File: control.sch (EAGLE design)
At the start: 4 parts, among them IC1 L293D, U1 AL5802-7, U4 AL5802-7

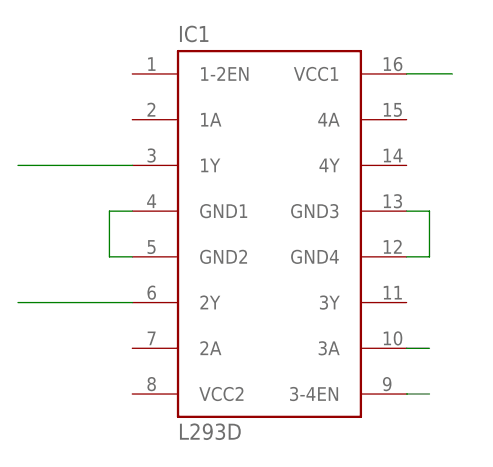
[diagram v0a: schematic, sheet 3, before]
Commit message: adds h bridge wirirng
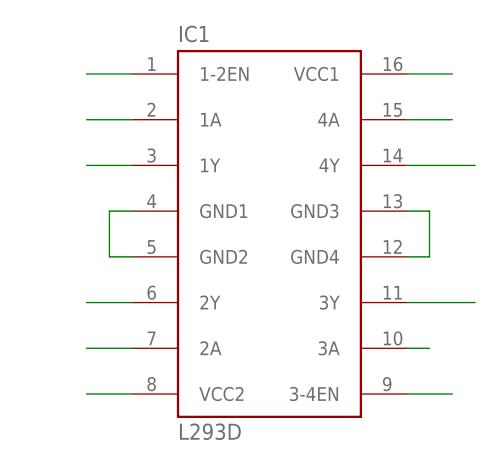
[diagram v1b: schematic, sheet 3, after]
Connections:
- net N$1 renamed M1A
- net N$6 renamed M1B
- net N$8 renamed SPEED2
- net N$9 renamed DIR2B
- new net DIR1A: IC1.1A
- new net DIR1B: IC1.2A
- new net DIR2A: IC1.4A
- new net M2A: IC1.4Y
- new net M2B: IC1.3Y
- new net SPEED1: IC1.1-2EN
- net 24V: now also IC1.VCC2
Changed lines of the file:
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@@
 </segment>
 </net>
-<net name="N$1" class="0">
+<net name="M1A" class="0">
 <segment>
 <pinref part="IC1" gate="G$1" pin="1Y"/>
-<wire x1="-5.08" y1="27.94" x2="-17.78" y2="27.94" width="0.1524" layer="91"/>
+<wire x1="-5.08" y1="27.94" x2="-10.16" y2="27.94" width="0.1524" layer="91"/>
 </segment>
 </net>
-<net name="N$6" class="0">
+<net name="M1B" class="0">
 <segment>
 <pinref part="IC1" gate="G$1" pin="2Y"/>
-<wire x1="-5.08" y1="12.7" x2="-17.78" y2="12.7" width="0.1524" layer="91"/>
+<wire x1="-5.08" y1="12.7" x2="-10.16" y2="12.7" width="0.1524" layer="91"/>
 </segment>
 </net>
-<net name="N$8" class="0">
+<net name="SPEED2" class="0">
 <segment>
 <pinref part="IC1" gate="G$1" pin="3-4EN"/>
-<wire x1="25.4" y1="2.54" x2="27.94" y2="2.54" width="0.1524" layer="91"/>
+<wire x1="25.4" y1="2.54" x2="30.48" y2="2.54" width="0.1524" layer="91"/>
 </segment>
 </net>
-<net name="N$9" class="0">
+<net name="DIR2B" class="0">
 <segment>
 <pinref part="IC1" gate="G$1" pin="3A"/>
@@
 </segment>
 </net>
+<net name="24V" class="0">
+<segment>
+<pinref part="IC1" gate="G$1" pin="VCC2"/>
+<wire x1="-5.08" y1="2.54" x2="-10.16" y2="2.54" width="0.1524" layer="91"/>
+</segment>
+</net>
+<net name="M2A" class="0">
+<segment>
+<pinref part="IC1" gate="G$1" pin="4Y"/>
+<wire x1="25.4" y1="27.94" x2="33.02" y2="27.94" width="0.1524" layer="91"/>
+</segment>
+</net>
+<net name="M2B" class="0">
+<segment>
+<pinref part="IC1" gate="G$1" pin="3Y"/>
+<wire x1="25.4" y1="12.7" x2="33.02" y2="12.7" width="0.1524" layer="91"/>
+</segment>
+</net>
+<net name="SPEED1" class="0">
+<segment>
+<pinref part="IC1" gate="G$1" pin="1-2EN"/>
+<wire x1="-5.08" y1="38.1" x2="-10.16" y2="38.1" width="0.1524" layer="91"/>
+</segment>
+</net>
+<net name="DIR1A" class="0">
+<segment>
+<pinref part="IC1" gate="G$1" pin="1A"/>
+<wire x1="-5.08" y1="33.02" x2="-10.16" y2="33.02" width="0.1524" layer="91"/>
+</segment>
+</net>
+<net name="DIR2A" class="0">
+<segment>
+<pinref part="IC1" gate="G$1" pin="4A"/>
+<wire x1="25.4" y1="33.02" x2="30.48" y2="33.02" width="0.1524" layer="91"/>
+</segment>
+</net>
+<net name="DIR1B" class="0">
+<segment>
+<pinref part="IC1" gate="G$1" pin="2A"/>
+<wire x1="-5.08" y1="7.62" x2="-10.16" y2="7.62" width="0.1524" layer="91"/>
+</segment>
+</net>

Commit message: adds LED driver
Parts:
- removed IC1: L293D, st-microelectronics:L293D
- removed U1, U4: AL5802-7, LED Driver:AL5802-7
- added C1: UVR0J102MPD1TA, Smile_Shade:UVR0J102MPD1TA
- added C2: ESK107M025AE3EA, Smile_Shade:ESK107M025AE3EA
- added R1, R10, R11, R12, R13, R14, R15, R16, R2, R3, R4, R5, R6, R7, R8, R9: RC0603FR-0710RL, LED Driver:RC0603FR-0710RL
- added U$10, U$12, U$14, U$16, U$18, U$20, U$22, U$24, U$26, U$28, U$30, U$32, U$34, U$4, U$6, U$8: 2N7002P, LED Driver:2N7002P
- added U$11, U$13, U$15, U$17, U$19, U$21, U$23, U$25, U$27, U$29, U$3, U$31, U$33, U$5, U$7, U$9: NUD4011DR2G, LED Driver:NUD4011DR2G
- added U$2: L293DNE, LED Driver:L293DNE
- added U$35: LM2576HVT-5.0/NOPB, LED Driver:LM2576HVT-5.0/NOPB
- added U$36: SRN8040-101M, Smile_Shade:SRN8040-101M
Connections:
- removed net DIR1B: IC1.2A
- removed net DIR2A: IC1.4A
- removed net DIR2B: IC1.3A
- removed net LED1: U1.OUT
- removed net M1A: IC1.1Y
- removed net M2B: IC1.3Y
- removed net SPEED1: IC1.1-2EN
- removed net SPEED2: IC1.3-4EN
- new net 48V: C2.11, R1.22, R10.22, R11.22, R12.22, R13.22, R14.22, R15.22, R16.22, R2.22, R3.22, R4.22, R5.22, R6.22, R7.22, R8.22, R9.22, U$11.VIN, U$13.VIN, U$15.VIN, U$17.VIN, U$19.VIN, U$21.VIN, U$23.VIN, U$25.VIN, U$27.VIN, U$29.VIN, U$3.VIN, U$31.VIN, U$33.VIN, U$5.VIN, U$7.VIN, U$9.VIN
- new net LEDSTR_1: U$17.LED1, U$17.LED2, U$17.LED3, U$17.LED4
- new net LEDSTR_10: U$21.LED1, U$21.LED2, U$21.LED3, U$21.LED4
- new net LEDSTR_11: U$23.LED1, U$23.LED2, U$23.LED3, U$23.LED4
- new net LEDSTR_12: U$25.LED1, U$25.LED2, U$25.LED3, U$25.LED4
- new net LEDSTR_13: U$27.LED1, U$27.LED2, U$27.LED3, U$27.LED4
- new net LEDSTR_14: U$29.LED1, U$29.LED2, U$29.LED3, U$29.LED4
- new net LEDSTR_15: U$31.LED1, U$31.LED2, U$31.LED3, U$31.LED4
- new net LEDSTR_16: U$33.LED1, U$33.LED2, U$33.LED3, U$33.LED4
- new net LEDSTR_2: U$3.LED1, U$3.LED2, U$3.LED3, U$3.LED4
- new net LEDSTR_3: U$5.LED1, U$5.LED2, U$5.LED3, U$5.LED4
- new net LEDSTR_4: U$7.LED1, U$7.LED2, U$7.LED3, U$7.LED4
- new net LEDSTR_5: U$9.LED1, U$9.LED2, U$9.LED3, U$9.LED4
- new net LEDSTR_6: U$11.LED1, U$11.LED2, U$11.LED3, U$11.LED4
- new net LEDSTR_7: U$13.LED1, U$13.LED2, U$13.LED3, U$13.LED4
- new net LEDSTR_8: U$15.LED1, U$15.LED2, U$15.LED3, U$15.LED4
- new net LEDSTR_9: U$19.LED1, U$19.LED2, U$19.LED3, U$19.LED4
- new net N$1: U$3.PWM, U$4.SOURCE
- new net N$10: R5.11, U$11.REXT
- new net N$11: U$13.PWM, U$14.SOURCE
- new net N$12: R6.11, U$13.REXT
- new net N$13: U$15.PWM, U$16.SOURCE
- new net N$14: R7.11, U$15.REXT
- new net N$15: U$17.PWM, U$18.SOURCE
- new net N$16: R8.11, U$17.REXT
- new net N$17: U$19.PWM, U$20.SOURCE
- new net N$18: R9.11, U$19.REXT
- new net N$19: U$21.PWM, U$22.SOURCE
- new net N$20: R10.11, U$21.REXT
- new net N$21: U$23.PWM, U$24.SOURCE
- new net N$22: R11.11, U$23.REXT
- new net N$23: U$25.PWM, U$26.SOURCE
- new net N$24: R12.11, U$25.REXT
- new net N$25: U$27.PWM, U$28.SOURCE
- new net N$26: R13.11, U$27.REXT
- new net N$27: U$29.PWM, U$30.SOURCE
- new net N$28: R14.11, U$29.REXT
- new net N$29: U$31.PWM, U$32.SOURCE
- new net N$30: R15.11, U$31.REXT
- new net N$31: U$33.PWM, U$34.SOURCE
- new net N$32: R16.11, U$33.REXT
- new net N$33: U$35.OUT, U$36.1
- new net N$34: C2.22, U$35.VIN
- new net N$6: R3.11, U$7.REXT
- new net N$8: R4.11, U$9.REXT
- new net N$9: U$11.PWM, U$12.SOURCE
- new net PWMLED1: U$4.GATE
- new net PWMLED10: U$22.GATE
- new net PWMLED11: U$24.GATE
- new net PWMLED12: U$26.GATE
- new net PWMLED13: U$28.GATE
- new net PWMLED14: U$30.GATE
- new net PWMLED15: U$32.GATE
- new net PWMLED16: U$34.GATE
- new net PWMLED2: U$6.GATE
- new net PWMLED3: U$8.GATE
- new net PWMLED4: U$10.GATE
- new net PWMLED5: U$12.GATE
- new net PWMLED6: U$14.GATE
- new net PWMLED7: U$16.GATE
- new net PWMLED8: U$18.GATE
- new net PWMLED9: U$20.GATE
- net 24V: now also U$2.VCC2; no longer IC1.VCC2, U1.BIAS, U4.BIAS
- net 5V: now also C1.22, U$1.CHG-IN, U$2.VCC1, U$35.FB, U$36.2; no longer IC1.VCC1
- net DIR1A: now also U$2.2A; no longer IC1.1A
- net GND: now also C1.11, U$10.DRAIN, U$12.DRAIN, U$14.DRAIN, U$16.DRAIN, U$18.DRAIN, U$2.HEATSINKANDGROUND, U$2.HEATSINKANDGROUND_2, U$2.HEATSINKANDGROUND_3, U$2.HEATSINKANDGROUND_4, U$20.DRAIN, U$22.DRAIN, U$24.DRAIN, U$26.DRAIN, U$28.DRAIN, U$30.DRAIN, U$32.DRAIN, U$34.DRAIN, U$35.!ON/OFF, U$35.GND, U$4.DRAIN, U$6.DRAIN, U$8.DRAIN; no longer IC1.GND1, IC1.GND2, IC1.GND3, IC1.GND4, U1.GND, U4.GND
- net M1B: now also U$2.2Y; no longer IC1.2Y
- net M2A: now also U$2.4Y; no longer IC1.4Y
- net N$2: now also R1.11, U$3.REXT; no longer U4.FB, U4.REXT
- net N$3: now also U$5.PWM, U$6.SOURCE; no longer U1.FB, U1.REXT
- net N$4: now also R2.11, U$5.REXT; no longer U4.EN
- net N$5: now also U$7.PWM, U$8.SOURCE; no longer U1.EN
- net N$7: now also U$10.SOURCE, U$9.PWM; no longer U4.OUT

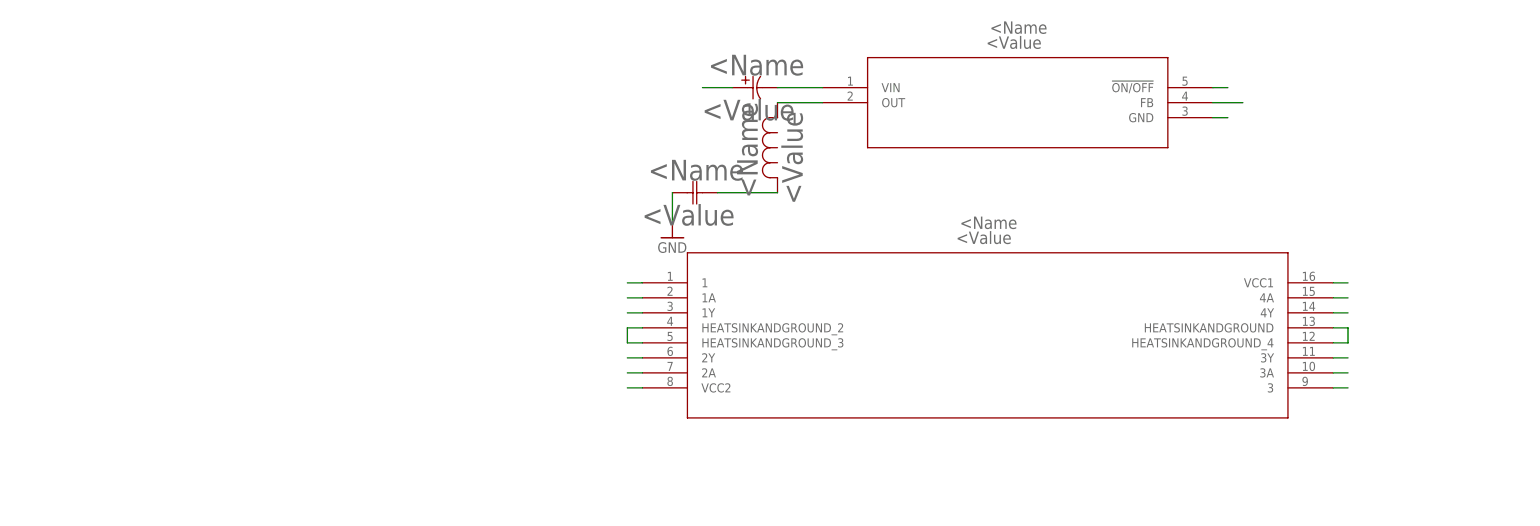
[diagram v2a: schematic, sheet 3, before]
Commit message: adds PWM
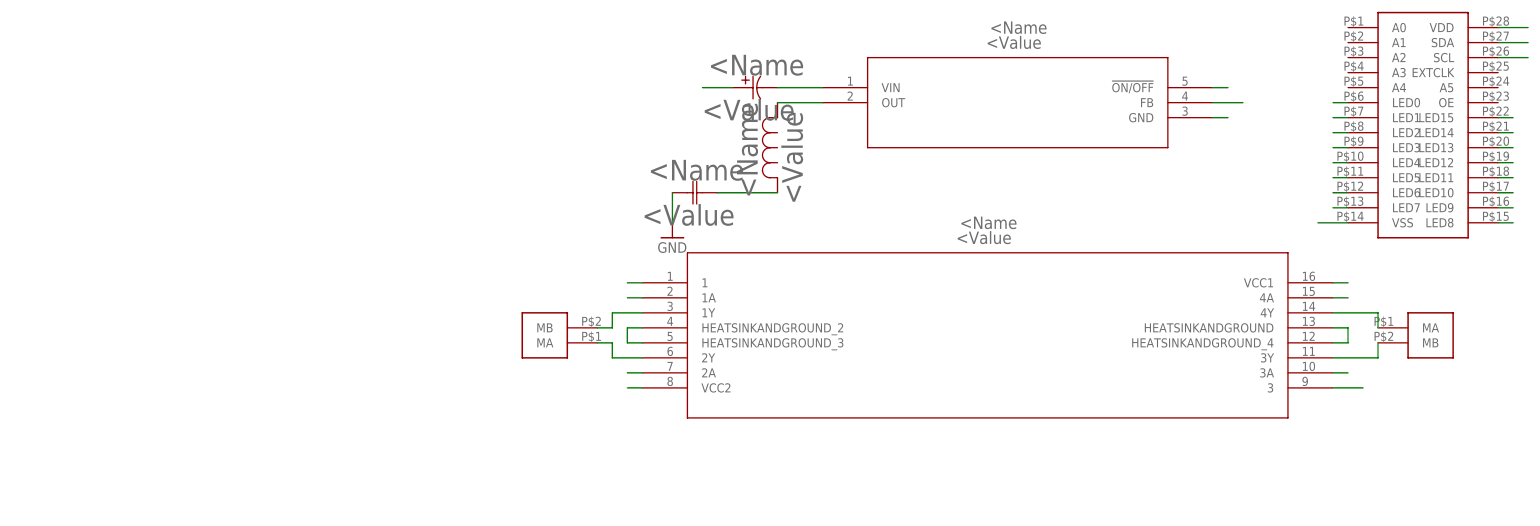
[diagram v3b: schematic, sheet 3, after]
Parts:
- added R17, R18: RC0603FR-0710RL, LED Driver:RC0603FR-0710RL
- added U$37: PCA9685PW/Q900, Smile_Shade:PCA9685PW/Q900
- added U$38, U$39: MOTORCONNECTOR, Smile_Shade:MOTORCONNECTOR
- added U$40, U$42: NUD4011DR2G, LED Driver:NUD4011DR2G
- added U$41, U$43: 2N7002P, LED Driver:2N7002P
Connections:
- removed net PWMLED1: U$4.GATE
- removed net PWMLED10: U$22.GATE
- removed net PWMLED11: U$24.GATE
- removed net PWMLED12: U$26.GATE
- removed net PWMLED13: U$28.GATE
- removed net PWMLED14: U$30.GATE
- removed net PWMLED15: U$32.GATE
- removed net PWMLED16: U$34.GATE
- removed net PWMLED2: U$6.GATE
- removed net PWMLED3: U$8.GATE
- removed net PWMLED4: U$10.GATE
- removed net PWMLED5: U$12.GATE
- removed net PWMLED6: U$14.GATE
- removed net PWMLED7: U$16.GATE
- removed net PWMLED8: U$18.GATE
- removed net PWMLED9: U$20.GATE
- new net 48: R17.22, U$40.VIN
- new net LEDSTR_17: U$40.LED1, U$40.LED2, U$40.LED3, U$40.LED4
- new net LEDSTR_18: U$42.LED1, U$42.LED2, U$42.LED3, U$42.LED4
- new net M0: U$1.PWM0, U$2.1
- new net M1: U$1.PWM1, U$2.3
- new net M1A: U$2.1Y, U$38.MB
- new net M2B: U$2.3Y, U$39.MB
- new net N$35: U$40.PWM, U$41.SOURCE
- new net N$36: R17.11, U$40.REXT
- new net N$37: U$42.PWM, U$43.SOURCE
- new net N$38: R18.11, U$42.REXT
- new net SCK: U$1.TWI1-SCK, U$37.SCL
- new net SDA: U$1.TWI1-SDA, U$37.SDA
- new net ZN0: U$18.GATE, U$37.LED0
- new net ZN1: U$37.LED1, U$4.GATE
- new net ZN10: U$30.GATE, U$37.LED10
- new net ZN11: U$28.GATE, U$37.LED11
- new net ZN12: U$26.GATE, U$37.LED12
- new net ZN13: U$20.GATE, U$37.LED13
- new net ZN14: U$22.GATE, U$37.LED14
- new net ZN15: U$24.GATE, U$37.LED15
- new net ZN16: U$43.GATE
- new net ZN2: U$37.LED2, U$6.GATE
- new net ZN3: U$37.LED3, U$8.GATE
- new net ZN4: U$14.GATE, U$37.LED4
- new net ZN5: U$12.GATE, U$37.LED5
- new net ZN6: U$10.GATE, U$37.LED6
- new net ZN7: U$16.GATE, U$37.LED7
- new net ZN8: U$34.GATE, U$37.LED8, U$41.GATE
- new net ZN9: U$32.GATE, U$37.LED9
- net 48V: now also R18.22, U$42.VIN
- net 5V: now also U$37.VDD
- net GND: now also U$37.VSS, U$41.DRAIN, U$43.DRAIN
- net M1B: now also U$38.MA
- net M2A: now also U$39.MA

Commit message: Revert "Merge remote-tracking branch 'refs/remotes/origin/master' into new-layout"
This reverts commit d786cf153478cbc5e1d0f0cbdb23b775e7a3effd.
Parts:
- U$39: value MOTORCONNECTOR -> SFV18R-3STBE1HLF; device Smile_Shade:MOTORCONNECTOR -> Smile_Shade:SFV18R-3STBE1HLF
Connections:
- net LEDSTR_1: now also U$39.P$18
- net LEDSTR_10: now also U$39.P$9
- net LEDSTR_11: now also U$39.P$10
- net LEDSTR_12: now also U$39.P$7
- net LEDSTR_13: now also U$39.P$6
- net LEDSTR_14: now also U$39.P$5
- net LEDSTR_15: now also U$39.P$4
- net LEDSTR_16: now also U$39.P$3
- net LEDSTR_17: now also U$39.P$1
- net LEDSTR_18: now also U$39.P$2
- net LEDSTR_2: now also U$39.P$17
- net LEDSTR_3: now also U$39.P$16
- net LEDSTR_4: now also U$39.P$15
- net LEDSTR_5: now also U$39.P$12
- net LEDSTR_6: now also U$39.P$13
- net LEDSTR_7: now also U$39.P$14
- net LEDSTR_8: now also U$39.P$11
- net LEDSTR_9: now also U$39.P$8
- net M1A: no longer U$38.MB
- net M1B: no longer U$38.MA
- net M2A: now also U$38.MA; no longer U$39.MA
- net M2B: now also U$38.MB; no longer U$39.MB
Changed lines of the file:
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@@
 <part name="U$37" library="Smile_Shade" deviceset="PCA9685PW/Q900" device=""/>
 <part name="U$38" library="Smile_Shade" deviceset="MOTORCONNECTOR" device=""/>
-<part name="U$39" library="Smile_Shade" deviceset="MOTORCONNECTOR" device=""/>
 <part name="U$40" library="LED Driver" deviceset="NUD4011DR2G" device=""/>
 <part name="U$41" library="LED Driver" deviceset="2N7002P" device=""/>
@@
 <part name="U$43" library="LED Driver" deviceset="2N7002P" device=""/>
 <part name="R18" library="LED Driver" deviceset="RC0603FR-0710RL" device=""/>
+<part name="U$39" library="Smile_Shade" deviceset="SFV18R-3STBE1HLF" device=""/>
 </parts>
 <sheets>
@@
 <instance part="U$43" gate="G$1" x="55.88" y="-58.42"/>
 <instance part="R18" gate="A" x="30.48" y="-45.72"/>
+<instance part="U$39" gate="G$1" x="-43.18" y="60.96" rot="R90"/>
 </instances>
 <busses>
@@
 <wire x1="22.86" y1="101.6" x2="25.4" y2="101.6" width="0.1524" layer="91"/>
 </segment>
+<segment>
+<pinref part="U$39" gate="G$1" pin="P$18"/>
+<wire x1="-38.1" y1="106.68" x2="-35.56" y2="106.68" width="0.1524" layer="91"/>
+</segment>
 </net>
 <net name="N$15" class="0">
@@
 <wire x1="73.66" y1="101.6" x2="76.2" y2="101.6" width="0.1524" layer="91"/>
 </segment>
+<segment>
+<wire x1="-38.1" y1="104.14" x2="-35.56" y2="104.14" width="0.1524" layer="91"/>
+<pinref part="U$39" gate="G$1" pin="P$17"/>
+<junction x="-38.1" y="104.14"/>
+</segment>
 </net>
 <net name="N$1" class="0">
@@
 <wire x1="121.92" y1="101.6" x2="124.46" y2="101.6" width="0.1524" layer="91"/>
 </segment>
+<segment>
+<wire x1="-38.1" y1="101.6" x2="-35.56" y2="101.6" width="0.1524" layer="91"/>
+<wire x1="-38.1" y1="101.6" x2="-35.56" y2="101.6" width="0.1524" layer="91"/>
+<pinref part="U$39" gate="G$1" pin="P$16"/>
+<junction x="-38.1" y="101.6"/>
+</segment>
 </net>
 <net name="N$3" class="0">
@@
 <wire x1="172.72" y1="101.6" x2="175.26" y2="101.6" width="0.1524" layer="91"/>
 </segment>
+<segment>
+<wire x1="-38.1" y1="99.06" x2="-35.56" y2="99.06" width="0.1524" layer="91"/>
+<pinref part="U$39" gate="G$1" pin="P$15"/>
+<junction x="-38.1" y="99.06"/>
+</segment>
 </net>
 <net name="N$5" class="0">
@@
 <wire x1="22.86" y1="66.04" x2="25.4" y2="66.04" width="0.1524" layer="91"/>
 </segment>
+<segment>
+<pinref part="U$39" gate="G$1" pin="P$12"/>
+<wire x1="-38.1" y1="91.44" x2="-35.56" y2="91.44" width="0.1524" layer="91"/>
+</segment>
 </net>
 <net name="N$7" class="0">
@@
 <wire x1="73.66" y1="66.04" x2="76.2" y2="66.04" width="0.1524" layer="91"/>
 </segment>
+<segment>
+<pinref part="U$39" gate="G$1" pin="P$13"/>
+<wire x1="-38.1" y1="93.98" x2="-35.56" y2="93.98" width="0.1524" layer="91"/>
+</segment>
 </net>
 <net name="N$9" class="0">
@@
 <wire x1="121.92" y1="66.04" x2="124.46" y2="66.04" width="0.1524" layer="91"/>
 </segment>
+<segment>
+<wire x1="-38.1" y1="96.52" x2="-35.56" y2="96.52" width="0.1524" layer="91"/>
+<pinref part="U$39" gate="G$1" pin="P$14"/>
+<junction x="-38.1" y="96.52"/>
+</segment>
 </net>
 <net name="N$11" class="0">
@@
 <wire x1="172.72" y1="66.04" x2="175.26" y2="66.04" width="0.1524" layer="91"/>
 </segment>
+<segment>
+<pinref part="U$39" gate="G$1" pin="P$11"/>
+<wire x1="-38.1" y1="88.9" x2="-35.56" y2="88.9" width="0.1524" layer="91"/>
+</segment>
 </net>
 <net name="N$13" class="0">
@@
 <wire x1="22.86" y1="30.48" x2="25.4" y2="30.48" width="0.1524" layer="91"/>
 </segment>
+<segment>
+<pinref part="U$39" gate="G$1" pin="P$8"/>
+<wire x1="-38.1" y1="81.28" x2="-35.56" y2="81.28" width="0.1524" layer="91"/>
+</segment>
 </net>
 <net name="N$17" class="0">
@@
 <wire x1="73.66" y1="30.48" x2="76.2" y2="30.48" width="0.1524" layer="91"/>
 </segment>
+<segment>
+<pinref part="U$39" gate="G$1" pin="P$9"/>
+<wire x1="-38.1" y1="83.82" x2="-35.56" y2="83.82" width="0.1524" layer="91"/>
+</segment>
 </net>
 <net name="N$19" class="0">
@@
 <wire x1="121.92" y1="30.48" x2="124.46" y2="30.48" width="0.1524" layer="91"/>
 </segment>
+<segment>
+<pinref part="U$39" gate="G$1" pin="P$10"/>
+<wire x1="-38.1" y1="86.36" x2="-35.56" y2="86.36" width="0.1524" layer="91"/>
+</segment>
 </net>
 <net name="N$21" class="0">
@@
 <wire x1="172.72" y1="30.48" x2="175.26" y2="30.48" width="0.1524" layer="91"/>
 </segment>
+<segment>
+<pinref part="U$39" gate="G$1" pin="P$7"/>
+<wire x1="-38.1" y1="78.74" x2="-35.56" y2="78.74" width="0.1524" layer="91"/>
+</segment>
 </net>
 <net name="N$23" class="0">
@@
 <wire x1="22.86" y1="-5.08" x2="25.4" y2="-5.08" width="0.1524" layer="91"/>
 </segment>
+<segment>
+<pinref part="U$39" gate="G$1" pin="P$6"/>
+<wire x1="-38.1" y1="76.2" x2="-35.56" y2="76.2" width="0.1524" layer="91"/>
+</segment>
 </net>
 <net name="N$25" class="0">
@@
 <wire x1="73.66" y1="-5.08" x2="76.2" y2="-5.08" width="0.1524" layer="91"/>
 </segment>
+<segment>
+<pinref part="U$39" gate="G$1" pin="P$5"/>
+<wire x1="-38.1" y1="73.66" x2="-35.56" y2="73.66" width="0.1524" layer="91"/>
+</segment>
 </net>
 <net name="N$27" class="0">
@@
 <wire x1="121.92" y1="-5.08" x2="124.46" y2="-5.08" width="0.1524" layer="91"/>
 </segment>
+<segment>
+<pinref part="U$39" gate="G$1" pin="P$4"/>
+<wire x1="-38.1" y1="71.12" x2="-35.56" y2="71.12" width="0.1524" layer="91"/>
+</segment>
 </net>
 <net name="N$29" class="0">
@@
 <wire x1="172.72" y1="-5.08" x2="175.26" y2="-5.08" width="0.1524" layer="91"/>
 </segment>
+<segment>
+<pinref part="U$39" gate="G$1" pin="P$3"/>
+<wire x1="-38.1" y1="68.58" x2="-35.56" y2="68.58" width="0.1524" layer="91"/>
+</segment>
 </net>
 <net name="N$31" class="0">
@@
 <wire x1="22.86" y1="-40.64" x2="25.4" y2="-40.64" width="0.1524" layer="91"/>
 </segment>
+<segment>
+<pinref part="U$39" gate="G$1" pin="P$1"/>
+<wire x1="-38.1" y1="63.5" x2="-35.56" y2="63.5" width="0.1524" layer="91"/>
+</segment>
 </net>
 <net name="N$35" class="0">
@@
 <wire x1="73.66" y1="-40.64" x2="76.2" y2="-40.64" width="0.1524" layer="91"/>
 </segment>
+<segment>
+<pinref part="U$39" gate="G$1" pin="P$2"/>
+<wire x1="-38.1" y1="66.04" x2="-35.56" y2="66.04" width="0.1524" layer="91"/>
+</segment>
 </net>
 <net name="N$37" class="0">
@@
 <instance part="C2" gate="A" x="104.14" y="68.58"/>
 <instance part="U$37" gate="G$1" x="213.36" y="43.18"/>
-<instance part="U$38" gate="G$1" x="76.2" y="25.4" rot="R180"/>
-<instance part="U$39" gate="G$1" x="218.44" y="27.94"/>
+<instance part="U$38" gate="G$1" x="218.44" y="27.94"/>
 </instances>
 <busses>
@@
 <segment>
 <wire x1="83.82" y1="30.48" x2="83.82" y2="27.94" width="0.1524" layer="91"/>
-<pinref part="U$38" gate="G$1" pin="MB"/>
-<wire x1="83.82" y1="27.94" x2="81.28" y2="27.94" width="0.1524" layer="91"/>
 <pinref part="U$2" gate="A" pin="1Y"/>
 <wire x1="83.82" y1="30.48" x2="88.9" y2="30.48" width="0.1524" layer="91"/>
@@
 <net name="M2B" class="0">
 <segment>
-<pinref part="U$39" gate="G$1" pin="MB"/>
 <wire x1="213.36" y1="25.4" x2="213.36" y2="22.86" width="0.1524" layer="91"/>
 <pinref part="U$2" gate="A" pin="3Y"/>
 <wire x1="205.74" y1="22.86" x2="213.36" y2="22.86" width="0.1524" layer="91"/>
+<pinref part="U$38" gate="G$1" pin="MB"/>
 </segment>
 </net>
@@
 <wire x1="88.9" y1="22.86" x2="83.82" y2="22.86" width="0.1524" layer="91"/>
 <wire x1="83.82" y1="22.86" x2="83.82" y2="25.4" width="0.1524" layer="91"/>
-<pinref part="U$38" gate="G$1" pin="MA"/>
-<wire x1="83.82" y1="25.4" x2="81.28" y2="25.4" width="0.1524" layer="91"/>
 </segment>
 </net>
@@
 <segment>
 <pinref part="U$2" gate="A" pin="4Y"/>
-<pinref part="U$39" gate="G$1" pin="MA"/>
 <wire x1="205.74" y1="30.48" x2="213.36" y2="30.48" width="0.1524" layer="91"/>
 <wire x1="213.36" y1="30.48" x2="213.36" y2="27.94" width="0.1524" layer="91"/>
-</segment>
-</net>
+<pinref part="U$38" gate="G$1" pin="MA"/>
+</segment>
+</net>
